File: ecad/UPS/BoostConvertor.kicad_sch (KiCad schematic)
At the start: 24 parts

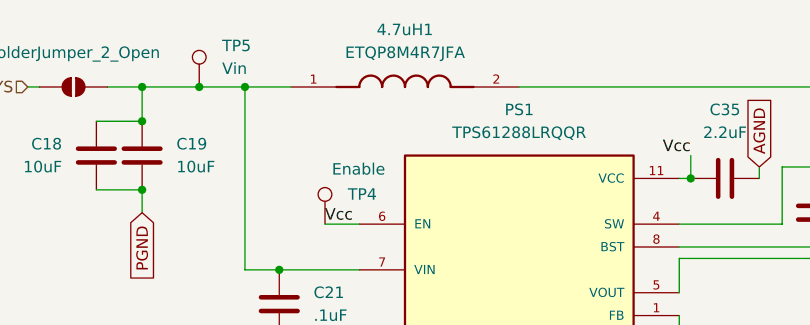
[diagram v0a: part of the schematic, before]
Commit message: Need to finish some traces, DRC warnings are keeping me from routing to the BQ,
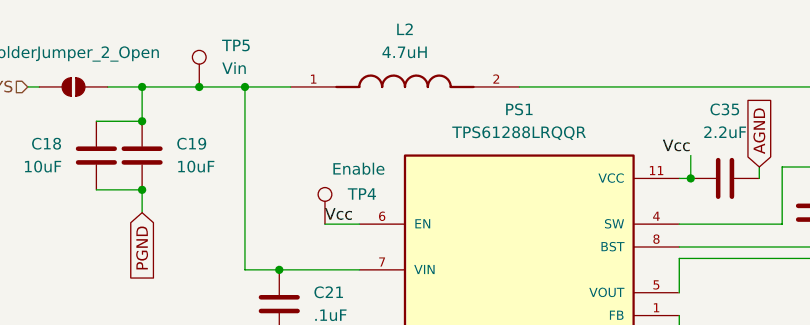
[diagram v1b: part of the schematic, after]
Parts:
- L2: renamed from 4.7uH1; value ETQP8M4R7JFA -> 4.7uH; footprint ETQP8M4R7JFA:IND_ETQP8M4R7JFA -> UPS:IND_ETQP8M4R7JFA
- PS1: footprint TPS61288LRQQR:CONV_TPS61288LRQQR -> UPS:CONV_TPS61288LRQQR
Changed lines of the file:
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@@
 		(dnp no)
 		(fields_autoplaced yes)
-		(property "Reference" "4.7uH1"
+		(property "Reference" "L2"
 			(at 92.71 45.72 0)
 			(effects
@@
 			)
 		)
-		(property "Value" "ETQP8M4R7JFA"
+		(property "Value" "4.7uH"
 			(at 92.71 48.26 0)
 			(effects
@@
 			)
 		)
-		(property "Footprint" "ETQP8M4R7JFA:IND_ETQP8M4R7JFA"
+		(property "Footprint" "UPS:IND_ETQP8M4R7JFA"
 			(at 92.71 52.07 0)
 			(effects
@@
 			(project ""
 				(path "/9d92b60a-4a6b-449c-b462-cab19e69d38c/66173f08-558e-4192-bd35-ba55c00529e3"
-					(reference "4.7uH1")
+					(reference "L2")
 					(unit 1)
 				)
@@
 			)
 		)
-		(property "Footprint" "TPS61288LRQQR:CONV_TPS61288LRQQR"
+		(property "Footprint" "UPS:CONV_TPS61288LRQQR"
 			(at 105.41 77.47 0)
 			(effects
